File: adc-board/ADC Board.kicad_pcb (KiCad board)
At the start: 4 copper layers, 92.7 x 83.8 mm, 125 parts, among them J1 BHR-44-HUA, J10 BootJumper, J2 ST-LINK/V2, J3 USART3, J4 USART1, J5 UE27AC5410H, J6 54601-908WPLF, J7 AltPowerInput, J8 USBPowerJumper, J9 USART2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

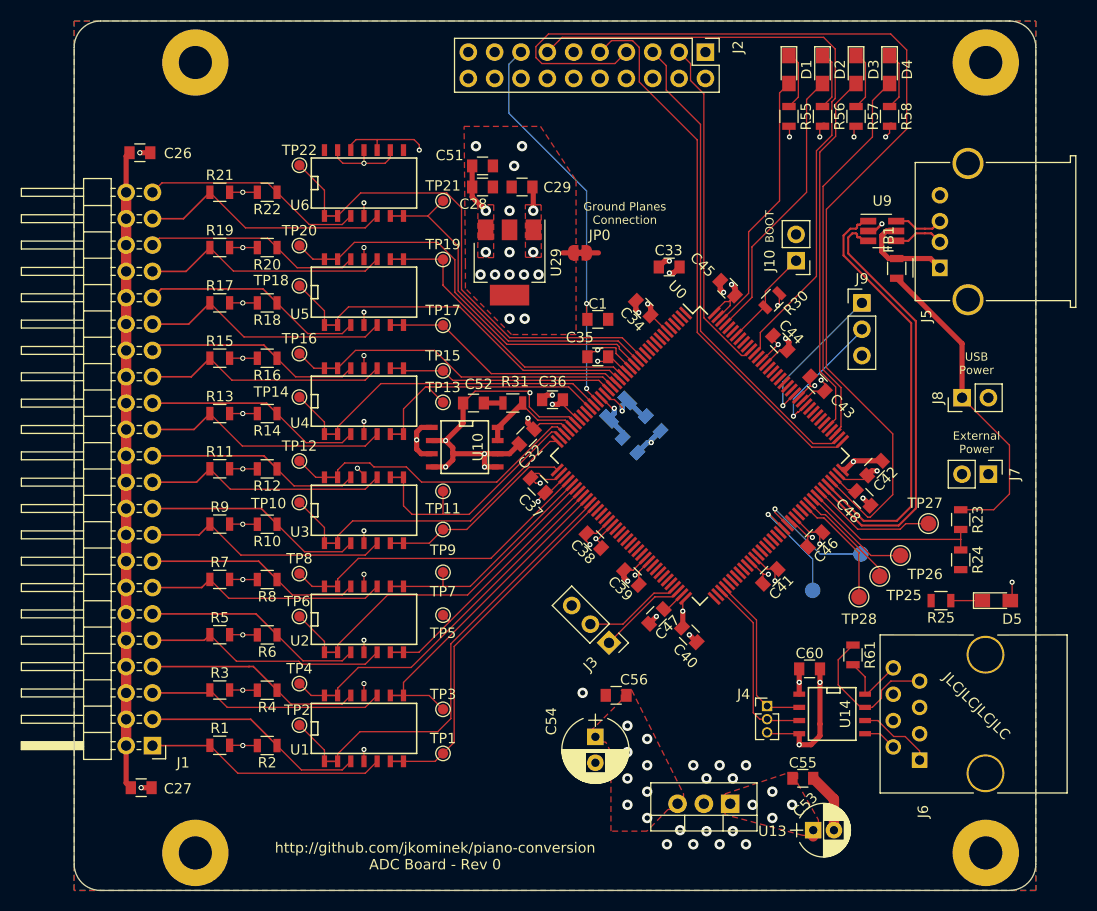
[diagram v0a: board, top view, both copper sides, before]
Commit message: Significant copper pour tweaks, and packing traces in tighter
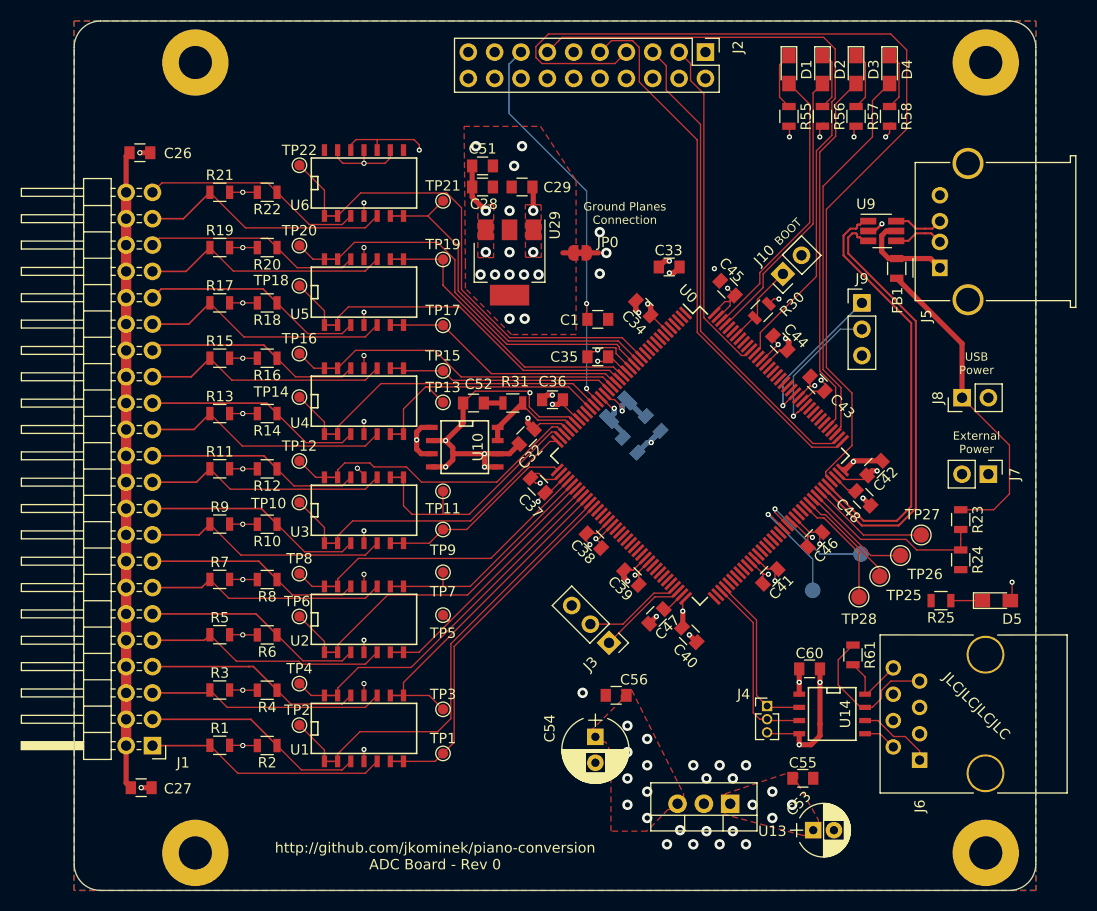
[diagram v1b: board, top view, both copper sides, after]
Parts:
- moved J10 1.80 mm to (100.1, 71.4), turned to 135 degrees
- moved R30 1.44 mm to (98.0, 74.9)
- moved TP27 1.30 mm to (113.4, 96.5)
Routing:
- net /JTMS: track 104.3 -> 94.4 mm
- net GNDD: track 76.4 -> 69.2 mm, vias 38 -> 41
- net /BOOT0: track 9.63 -> 7.83 mm
- net /LED1: track 25.5 -> 27.3 mm
- net /USART2_TX: track 12.8 -> 14.1 mm
- net Net-(TP27-Pad1): track 12.1 -> 11.4 mm
- net +5V: track 2.92 -> 2.32 mm

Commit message: Convert analog sensing over to transimpedance amplifiers
Also switched opamps for the TSSOP14 package, and replaced the
fancy voltage reference with a simple 2.0V regulator.
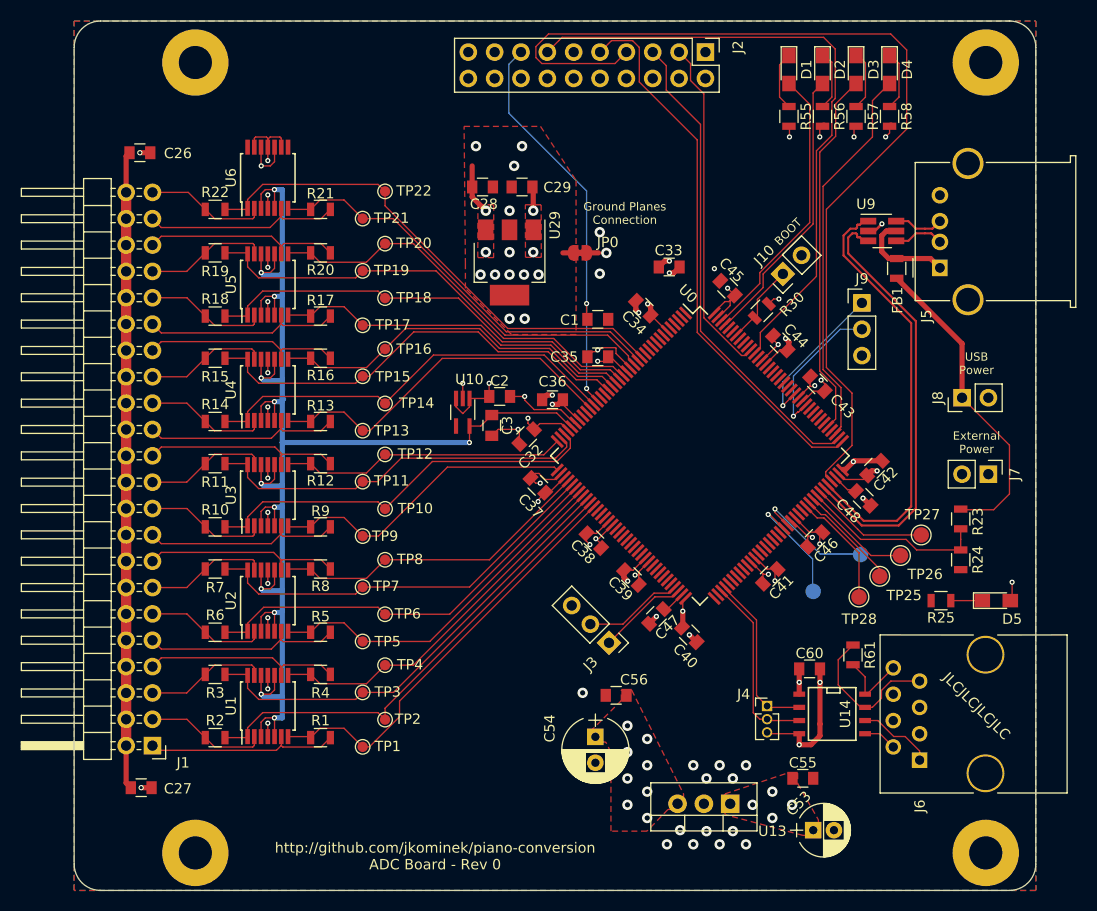
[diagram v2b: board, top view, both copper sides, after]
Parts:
- removed C49, C50: 4.3pF, Capacitors_SMD:C_0805
- removed C51, C52: 2.2uF, Capacitors_SMD:C_0805
- removed R31: 50, Resistors_SMD:R_0805
- removed Y1: NX3225GD-8.000M-EXS00A-CG04874, Crystals:Crystal_SMD_3215-2pin_3.2x1.5mm
- added C2: 2.2uF, Capacitors_SMD:C_0805, F.Cu at (72.8, 83.2)
- added C3: 2.2uF, Capacitors_SMD:C_0805, F.Cu at (72.0, 86.0)
- U1, U2, U3, U4, U5, U6: footprint SMD_Packages:SOIC-14_N -> Housings_SSOP:TSSOP-14_4.4x5mm_Pitch0.65mm
- U10: value MCP1501-20E/SN -> MIC5366-3.3YC5; footprint SMD_Packages:SOIC-8-N -> TO_SOT_Packages_SMD:SOT-353_SC-70-5_Handsoldering
- moved R21 9.85 mm to (55.5, 65.2), turned to 180 degrees
- moved R17 9.80 mm to (55.5, 75.4), turned to 180 degrees
- moved R13 9.74 mm to (55.5, 85.6), turned to 180 degrees
- moved R1 9.74 mm to (55.5, 116.1), turned to 180 degrees
- moved R9 9.72 mm to (55.5, 95.8), turned to 180 degrees
- moved R5 9.72 mm to (55.5, 105.9), turned to 180 degrees
- moved U1 9.49 mm to (50.4, 113.0), turned to 90 degrees
- moved U2 9.42 mm to (50.4, 102.9), turned to 90 degrees
- moved U3 9.36 mm to (50.4, 92.7), turned to 90 degrees
- moved U4 9.32 mm to (50.4, 82.5), turned to 90 degrees
- moved U5 9.29 mm to (50.4, 72.4), turned to 90 degrees
- moved U6 9.28 mm to (50.4, 62.1), turned to 90 degrees
- moved TP22 8.63 mm to (61.7, 63.4)
- moved TP4 8.44 mm to (61.7, 109.1)
- moved TP8 8.36 mm to (61.7, 98.9)
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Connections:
- R1 pad 2: GNDA -> /Sen1
- R10 pad 2: GNDA -> /Sen10
- R11 pad 2: GNDA -> /Sen11
- R12 pad 2: GNDA -> /Sen12
- R13 pad 2: GNDA -> /Sen13
- R14 pad 2: GNDA -> /Sen14
- R15 pad 2: GNDA -> /Sen15
- R16 pad 2: GNDA -> /Sen16
- R17 pad 2: GNDA -> /Sen17
- R18 pad 2: GNDA -> /Sen18
- R19 pad 2: GNDA -> /Sen19
- R2 pad 2: GNDA -> /Sen2
- R20 pad 2: GNDA -> /Sen20
- R21 pad 2: GNDA -> /Sen21
- R22 pad 2: GNDA -> /Sen22
- R3 pad 2: GNDA -> /Sen3
- R4 pad 2: GNDA -> /Sen4
- R5 pad 2: GNDA -> /Sen5
- R6 pad 2: GNDA -> /Sen6
- R7 pad 2: GNDA -> /Sen7
- R8 pad 2: GNDA -> /Sen8
- R9 pad 2: GNDA -> /Sen9
- U0 pad 23: Net-(C49-Pad2) -> (no net)
- U0 pad 24: Net-(C50-Pad2) -> (no net)
- U0 pad 34: /Sen12 -> /Sen10
- U0 pad 36: /Sen10 -> /Sen12
- U1 pad 10: /Analog Input/Sen3R -> /VREF+
- U1 pad 12: /Analog Input/Sen4R -> /VREF+
- U1 pad 13: /Sen4 -> /Analog Input/Sen3R
- U1 pad 14: /Sen4 -> /Sen3
- U1 pad 2: /Sen2 -> /Analog Input/Sen2R
- U1 pad 3: /Analog Input/Sen2R -> /VREF+
- U1 pad 5: /Analog Input/Sen1R -> /VREF+
- U1 pad 6: /Sen1 -> /Analog Input/Sen1R
- U1 pad 8: /Sen3 -> /Sen4
- U1 pad 9: /Sen3 -> /Analog Input/Sen4R
- U10 pad 4: GNDA -> (no net)
- U10 pad 5: GNDA -> /VREF+
- U2 pad 10: /Analog Input/Sen7R -> /VREF+
- U2 pad 12: /Analog Input/Sen8R -> /VREF+
- U2 pad 13: /Sen8 -> /Analog Input/Sen7R
- U2 pad 14: /Sen8 -> /Sen7
- U2 pad 2: /Sen6 -> /Analog Input/Sen6R
- U2 pad 3: /Analog Input/Sen6R -> /VREF+
- U2 pad 5: /Analog Input/Sen5R -> /VREF+
- U2 pad 6: /Sen5 -> /Analog Input/Sen5R
- U2 pad 8: /Sen7 -> /Sen8
- U2 pad 9: /Sen7 -> /Analog Input/Sen8R
- U3 pad 10: /Analog Input/Sen11R -> /VREF+
- U3 pad 12: /Analog Input/Sen12R -> /VREF+
- U3 pad 13: /Sen12 -> /Analog Input/Sen11R
- U3 pad 14: /Sen12 -> /Sen11
- U3 pad 2: /Sen10 -> /Analog Input/Sen10R
- U3 pad 3: /Analog Input/Sen10R -> /VREF+
- U3 pad 5: /Analog Input/Sen9R -> /VREF+
- U3 pad 6: /Sen9 -> /Analog Input/Sen9R
- U3 pad 8: /Sen11 -> /Sen12
- U3 pad 9: /Sen11 -> /Analog Input/Sen12R
- U4 pad 10: /Analog Input/Sen15R -> /VREF+
- U4 pad 12: /Analog Input/Sen16R -> /VREF+
- U4 pad 13: /Sen16 -> /Analog Input/Sen15R
- U4 pad 14: /Sen16 -> /Sen15
- U4 pad 2: /Sen14 -> /Analog Input/Sen14R
- U4 pad 3: /Analog Input/Sen14R -> /VREF+
- U4 pad 5: /Analog Input/Sen13R -> /VREF+
- U4 pad 6: /Sen13 -> /Analog Input/Sen13R
- U4 pad 8: /Sen15 -> /Sen16
- U4 pad 9: /Sen15 -> /Analog Input/Sen16R
- U5 pad 10: /Analog Input/Sen19R -> /VREF+
- U5 pad 12: /Analog Input/Sen20R -> /VREF+
- U5 pad 13: /Sen20 -> /Analog Input/Sen19R
- U5 pad 14: /Sen20 -> /Sen19
- U5 pad 2: /Sen18 -> /Analog Input/Sen18R
- U5 pad 3: /Analog Input/Sen18R -> /VREF+
- U5 pad 5: /Analog Input/Sen17R -> /VREF+
- U5 pad 6: /Sen17 -> /Analog Input/Sen17R
- U5 pad 8: /Sen19 -> /Sen20
- U5 pad 9: /Sen19 -> /Analog Input/Sen20R
- U6 pad 2: /Sen22 -> /Analog Input/Sen22R
- U6 pad 3: /Analog Input/Sen22R -> /VREF+
- U6 pad 5: /Analog Input/Sen21R -> /VREF+
- U6 pad 6: /Sen21 -> /Analog Input/Sen21R
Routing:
- net /VREF+: track 10.5 -> 148.5 mm, vias 0 -> 12
- net GNDA: track 79.4 -> 30.3 mm, vias 36 -> 23
- net /Sen15: track 21.9 -> 43.1 mm
- net /Sen7: track 22.9 -> 39.5 mm
- net /Sen19: track 28.6 -> 44.6 mm
- net /Sen3: track 31.9 -> 44.6 mm
- net /Sen11: track 25.3 -> 37.5 mm
- net /Analog Input/Sen19R: track 24.0 -> 11.9 mm
- net /Analog Input/Sen15R: track 23.8 -> 11.8 mm
- net /Analog Input/Sen11R: track 23.5 -> 11.8 mm
- net /Analog Input/Sen7R: track 23.2 -> 11.9 mm
- net /Analog Input/Sen3R: track 22.9 -> 11.8 mm
- net /Sen17: track 24.1 -> 35.1 mm
- net /Sen9: track 19.2 -> 30.0 mm
- net /Analog Input/Sen18R: track 21.6 -> 11.8 mm
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
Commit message: convert to surface mount caps for power filtration
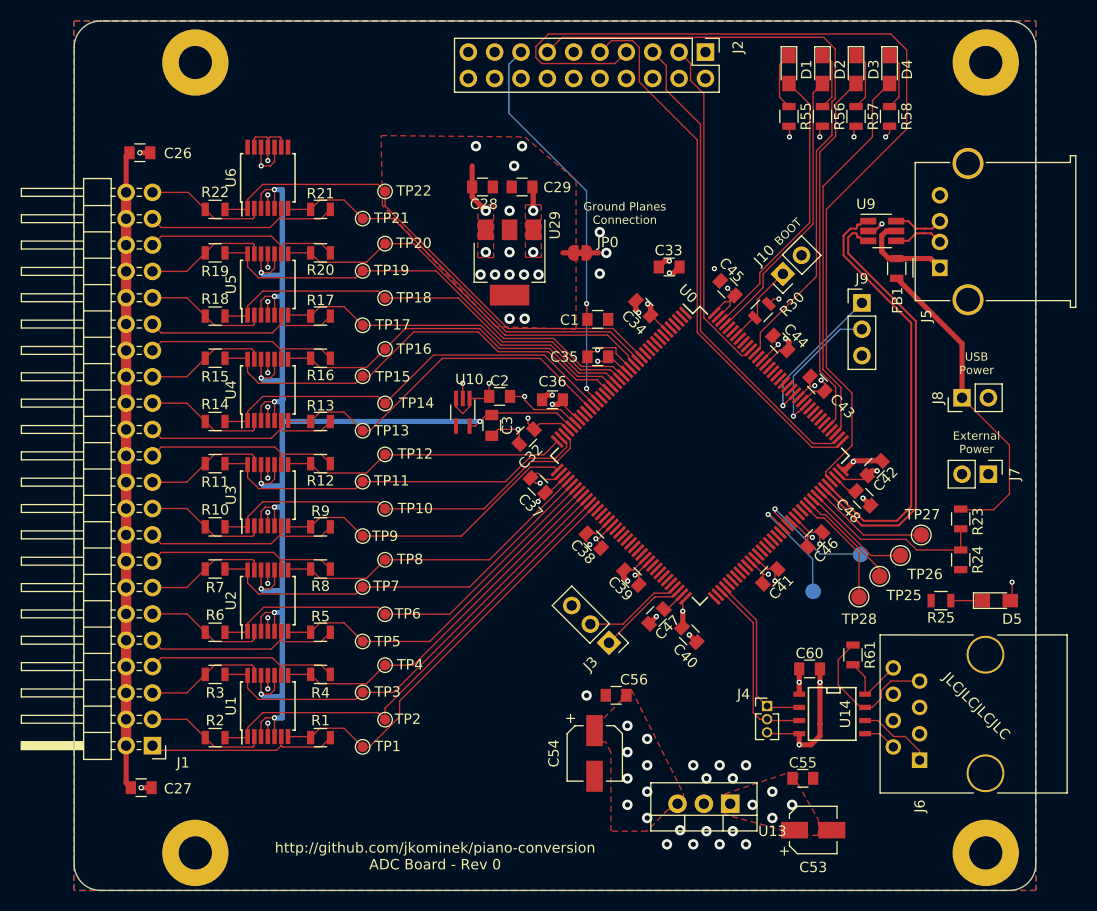
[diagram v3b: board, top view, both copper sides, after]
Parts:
- C53: footprint Capacitors_THT:CP_Radial_D5.0mm_P2.00mm -> Capacitors_SMD:CP_Elec_4x4.5
- C54: footprint Capacitors_THT:CP_Radial_D6.3mm_P2.50mm -> Capacitors_SMD:CP_Elec_5x5.3
- moved C54 1.60 mm to (81.9, 117.6)
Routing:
- net /VREF+: track 148.5 -> 148.0 mm

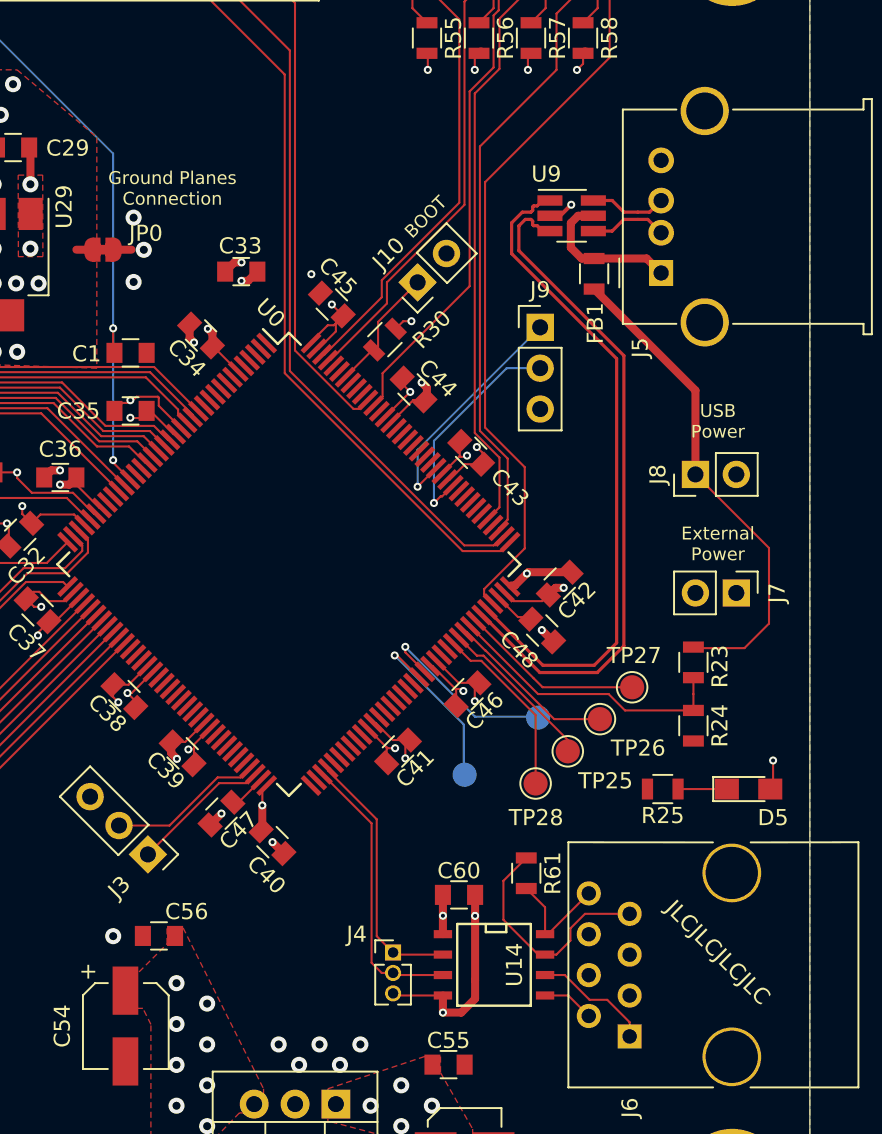
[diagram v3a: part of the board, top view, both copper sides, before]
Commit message: Fix swapped RS485 Z/Y pins. Add reset supervisor and 4 pin USB header.
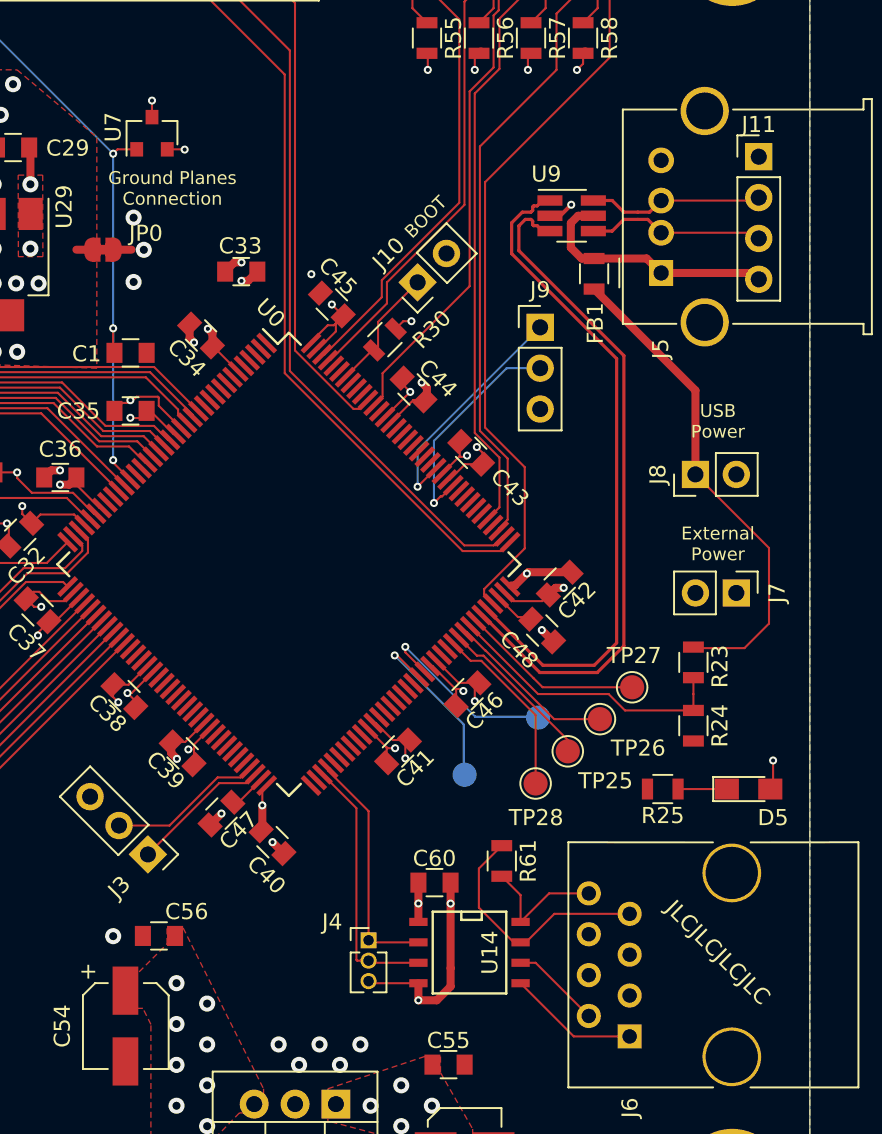
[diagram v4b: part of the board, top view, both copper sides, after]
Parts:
- added J11: USB Header, Pin_Headers:Pin_Header_Straight_1x04_Pitch2.54mm, F.Cu at (121.3, 63.6)
- added U7: MCP120-xxxxTT, TO_SOT_Packages_SMD:SOT-23, F.Cu at (83.6, 62.1)
- moved C60 1.70 mm to (101.1, 108.7)
- moved J4 1.70 mm to (97.0, 112.3)
- moved R61 1.70 mm to (105.3, 107.3)
- moved U14 1.70 mm to (103.3, 113.0)
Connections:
- U14 pad 5: /RS485/Z -> /RS485/Y
- U14 pad 6: /RS485/Y -> /RS485/Z
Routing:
- net Net-(FB1-Pad2): track 9.38 -> 15.6 mm
- net /USB_D-: track 4.86 -> 11.1 mm
- net /USB_D+: track 4.81 -> 11.0 mm
- net /RS485/Z: track 3.25 -> 5.61 mm
- net /NRST: track 39.2 -> 40.8 mm, vias 2 -> 3
- net /USART1_TX: track 17.7 -> 16.3 mm
- net /USART1_RX: track 16.4 -> 15.0 mm
- net /RS485/A: track 7.09 -> 8.48 mm
- net +3V3: track 54.1 -> 55.2 mm, vias 24 -> 25
- net GNDD: track 66.0 -> 67.0 mm, vias 40 -> 41
- net /RS485/Y: track 7.35 -> 8.15 mm
- net /RS485/B: track 14.7 -> 15.4 mm
